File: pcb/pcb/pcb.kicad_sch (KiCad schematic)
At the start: 24 parts, among them J1 UART, J2 Barrel_Jack, J3 Stepper, SW1 RESET, SW2 FLASH, U1 ESP32-WROOM-32, U2 TSR_1-2433

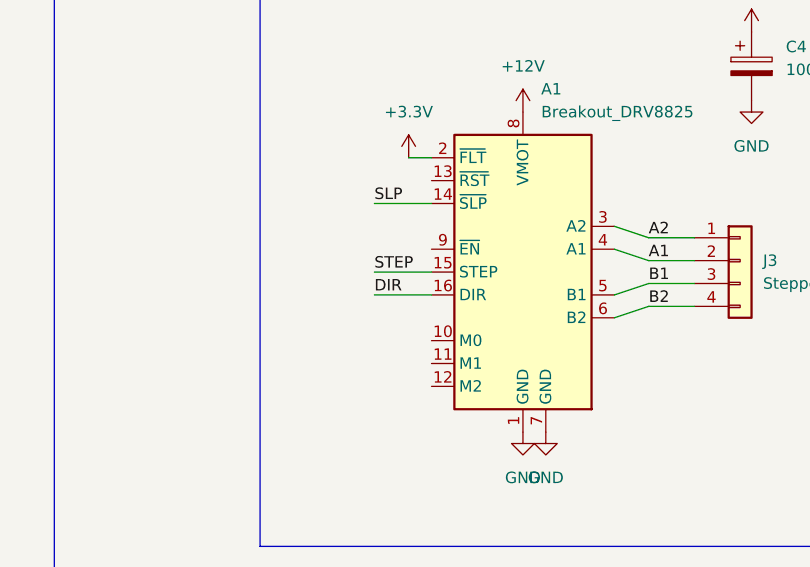
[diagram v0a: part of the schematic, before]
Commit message: Update pcb to fix bugs
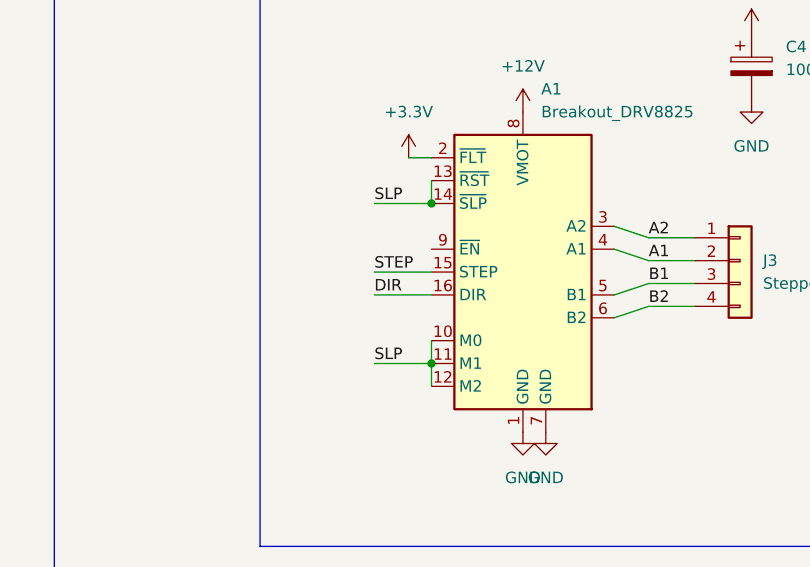
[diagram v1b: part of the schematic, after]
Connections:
- net SLP: now also A1.10 (M0), A1.11 (M1), A1.12 (M2), A1.13 (~{RST})
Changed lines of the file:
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@@
   (title_block
     (title "twilight")
-    (date "2022-01-30")
+    (date "2022-03-27")
     (rev "1.0")
     (comment 4 "ESP32 and DRV8825 based stepper motor controller")
@@
   (junction (at 186.69 60.96) (diameter 0) (color 0 0 0 0)
   )
+  (junction (at 181.61 120.65) (diameter 0) (color 0 0 0 0)
+  )
   (junction (at 186.69 45.72) (diameter 0) (color 0 0 0 0)
   )
@@
   (junction (at 234.95 45.72) (diameter 0) (color 0 0 0 0)
   )
+  (junction (at 181.61 138.43) (diameter 0) (color 0 0 0 0)
+  )
   (junction (at 27.94 100.33) (diameter 0) (color 0 0 0 0)
   )
@@
     (stroke (width 0) (type default) (color 0 0 0 0))
   )
+  (wire (pts (xy 175.26 138.43) (xy 181.61 138.43))
+    (stroke (width 0) (type default) (color 0 0 0 0))
+  )
+  (wire (pts (xy 181.61 118.11) (xy 181.61 120.65))
+    (stroke (width 0) (type default) (color 0 0 0 0))
+  )
   (wire (pts (xy 251.46 45.72) (xy 234.95 45.72))
     (stroke (width 0) (type default) (color 0 0 0 0))
@@
     (stroke (width 0) (type default) (color 0 0 0 0))
   )
+  (wire (pts (xy 181.61 135.89) (xy 181.61 138.43))
+    (stroke (width 0) (type default) (color 0 0 0 0))
+  )
   (wire (pts (xy 82.55 100.33) (xy 106.68 100.33))
     (stroke (width 0) (type default) (color 0 0 0 0))
@@
   )
   (wire (pts (xy 201.93 123.19) (xy 205.74 124.46))
+    (stroke (width 0) (type default) (color 0 0 0 0))
+  )
+  (wire (pts (xy 181.61 138.43) (xy 181.61 140.97))
     (stroke (width 0) (type default) (color 0 0 0 0))
   )
@@
     (effects (font (size 1.27 1.27)) (justify left bottom))
   )
+  (label "SLP" (at 175.26 138.43 0)
+    (effects (font (size 1.27 1.27)) (justify left bottom))
+  )

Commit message: Optimise routing
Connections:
- net +3V3: now also A1.10 (M0), A1.11 (M1), A1.12 (M2)
- net SLP: no longer A1.10 (M0), A1.11 (M1), A1.12 (M2)
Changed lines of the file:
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@@
-    (effects (font (size 1.27 1.27)) (justify left bottom))
-  )
-  (label "SLP" (at 175.26 138.43 0)
     (effects (font (size 1.27 1.27)) (justify left bottom))
   )
@@
       (effects (font (size 1.27 1.27)) hide)
     )
+  )
+  (symbol (lib_id "power:+3.3V") (at 175.26 138.43 0) (unit 1)
+    (in_bom yes) (on_board yes)
+    (property "Reference" "#PWR?" (id 0) (at 175.26 142.24 0)
+      (effects (font (size 1.27 1.27)) hide)
+    )
+    (property "Value" "" (id 1) (at 175.26 134.62 0))
+    (property "Footprint" "" (id 2) (at 175.26 138.43 0)
+      (effects (font (size 1.27 1.27)) hide)
+    )
+    (property "Datasheet" "" (id 3) (at 175.26 138.43 0)
+      (effects (font (size 1.27 1.27)) hide)
+    )
+    (pin "1")
   )
   (symbol (lib_id "power:GND") (at 101.6 73.66 0) (unit 1)
@@
       (reference "#PWR0104") (unit 1) (value "GND") (footprint "")
     )
+    (path "/39cc0ee6-3de2-4eb4-b08c-59f53e9be4df"
+      (reference "#PWR?") (unit 1) (value "+3.3V") (footprint "")
+    )
     (path "/b03e052e-fb2e-4d5e-ae41-d75f2a2ed3e5"
